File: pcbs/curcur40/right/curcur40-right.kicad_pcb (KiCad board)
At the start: 2 copper layers, 124.3 x 91.8 mm, 88 parts, among them U1 PMW3360DM-T2QU, U2 TLV74318PDBVR

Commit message: fix hole
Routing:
- net GNDR: track 248.1 -> 275.1 mm
- net /MISO: track 133.3 -> 133.8 mm
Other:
- outline, holes or cut-outs redrawn

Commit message: シルク文字
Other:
- board text added: "curcur40"

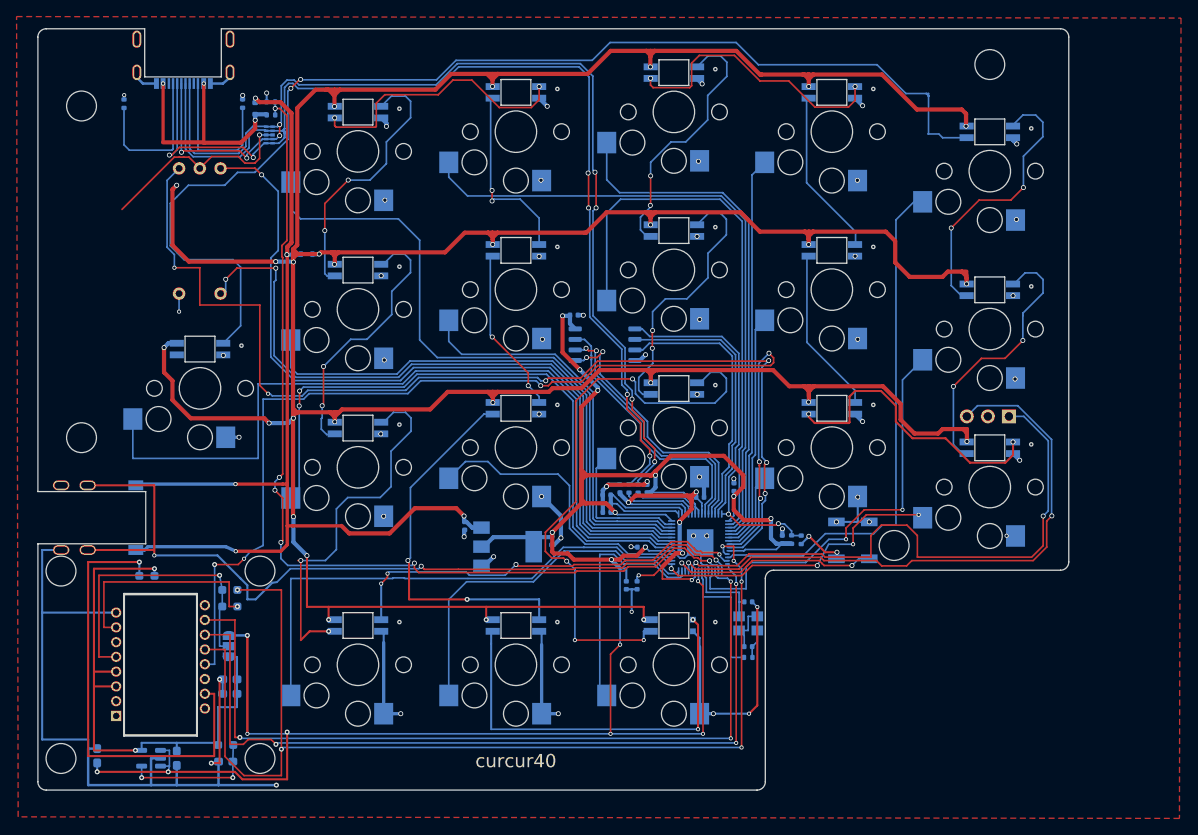
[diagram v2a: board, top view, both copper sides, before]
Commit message: fix(pcb): eliminate all ERC/DRC/parity warnings and ignored DRC checks on left and right PCBs
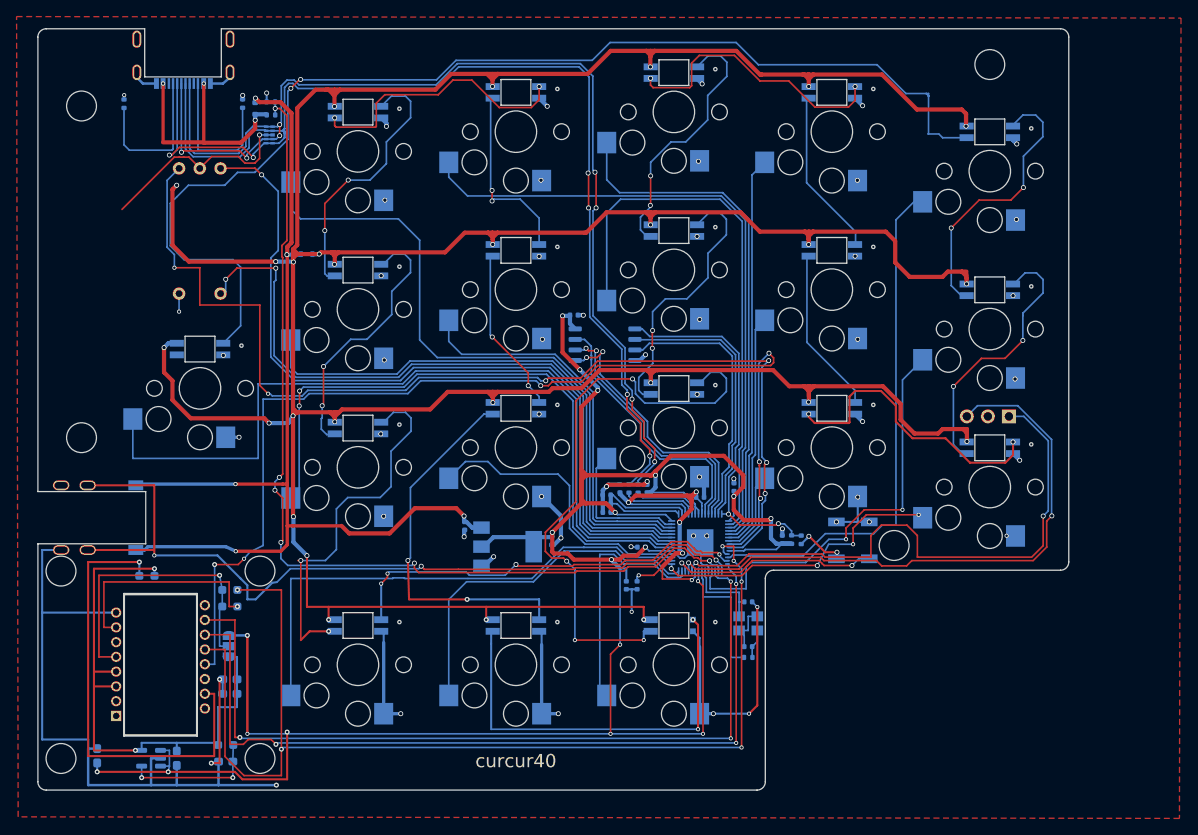
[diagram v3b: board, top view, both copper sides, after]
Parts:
- rLED9: footprint kbd_local:YS-SK6812MINI-E -> kbd_local:YS-SK6812MINI-E_rLED9
- rSW1: footprint kbd_local:keyswitch_choc12_hotswap_1u -> kbd_local:keyswitch_choc12_hotswap_1.5u
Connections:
- net +1V8_PMW renamed /+1V8_PMW
- net V_{IO} renamed /V_{IO}
- U1 pad 9: /MOTION -> unconnected-(U1-MOTION-Pad9)

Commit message: Refactor PCBs and schematics to use genuine KiCad 10.0 standard libraries and isolate PMW3360 VDDPIX
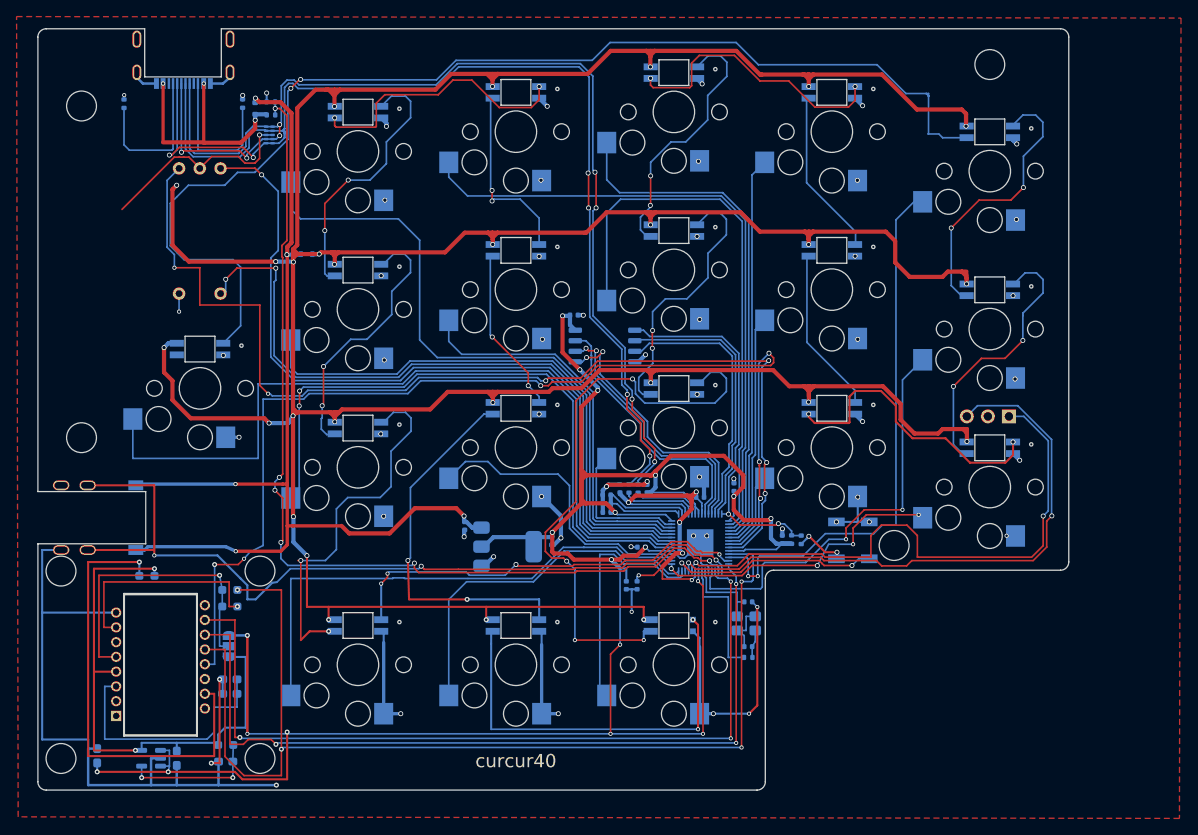
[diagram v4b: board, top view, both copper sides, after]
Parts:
- U1: footprint kbd_local:PMW3360DM-T2QU_16Pin -> kbd:PMW3360DM-T2QU_16Pin
- rEXLED2, rLED1, rLED10, rLED11, rLED12, rLED13, rLED14, rLED15, rLED16, rLED17, rLED18, rLED2, rLED3, rLED4, rLED5, rLED6, rLED7, rLED8: footprint kbd_local:YS-SK6812MINI-E -> kbd:YS-SK6812MINI-E
- rEXSW1: footprint kbd_local:CKW12 -> kbd:RotaryEncoder_Switch_CKW12
- rEXSW2, rSW10, rSW11, rSW12, rSW13, rSW14, rSW15, rSW16, rSW17, rSW18, rSW2, rSW3, rSW4, rSW5, rSW6, rSW7, rSW8, rSW9: footprint kbd_local:keyswitch_choc12_hotswap_1u -> kbd:keyswitch_choc12_hotswap_1u
- rJ1: footprint kbd_local:TYPE-C-31-M-13C -> kbd:USB_C_Receptacle_TYPE-C-31-M-13C
- rJ2: footprint kbd_local:PJ-398A-5A_PJ-399B-6A -> kbd:Jack_PJ-398A-5A_PJ-399B-6A
- rLED9: footprint kbd_local:YS-SK6812MINI-E_rLED9 -> kbd:YS-SK6812MINI-E_rLED9
- rSMDSW1, rSMDSW2: footprint kbd_local:TS-1088R-02026 -> kbd:TS-1088R-02026
- rSW1: footprint kbd_local:keyswitch_choc12_hotswap_1.5u -> kbd:keyswitch_choc12_hotswap_1.5u
- moved rY1 0.25 mm to (80.2, 47.4)
- moved rU4 0.16 mm to (63.1, 13.9)
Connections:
- C1 pad 1: /+1V8_PMW -> Net-(U1-VDDPIX)
- C2 pad 1: /+1V8_PMW -> Net-(U1-VDDPIX)
- U1 pad 3: /+1V8_PMW -> Net-(U1-VDDPIX)
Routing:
- net Net-(U1-VDDPIX): track 0.00 -> 30.4 mm
- net /KEY18: track 63.0 -> 67.1 mm, vias 0 -> 2
- net /+1V8_PMW: track 66.2 -> 65.1 mm
- net /MISO: track 133.8 -> 133.9 mm, vias 6 -> 4

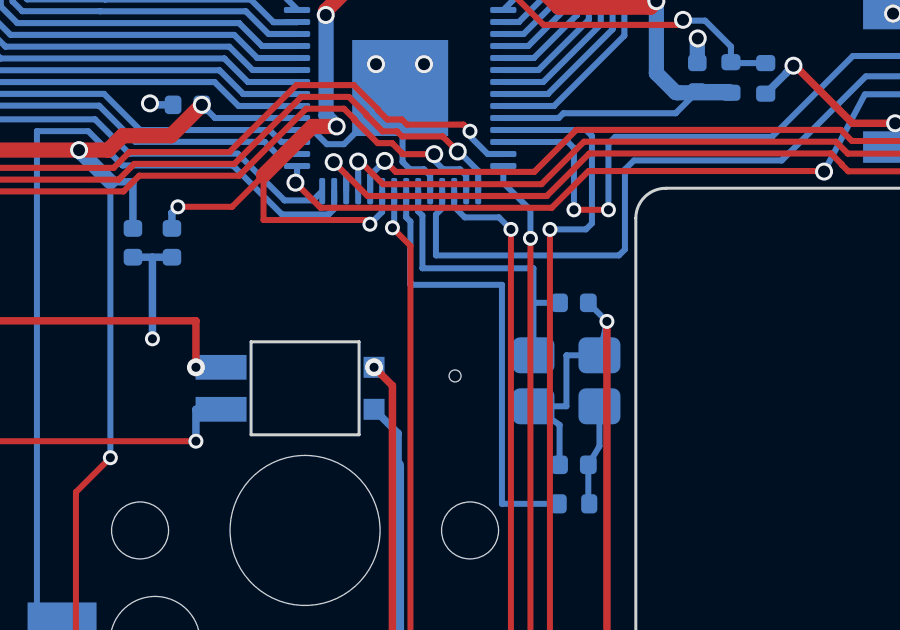
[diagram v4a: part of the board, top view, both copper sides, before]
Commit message: Clean up unused custom library files, fix fp-lib-table, and mark SWD headers J4/rJ4 as DNP
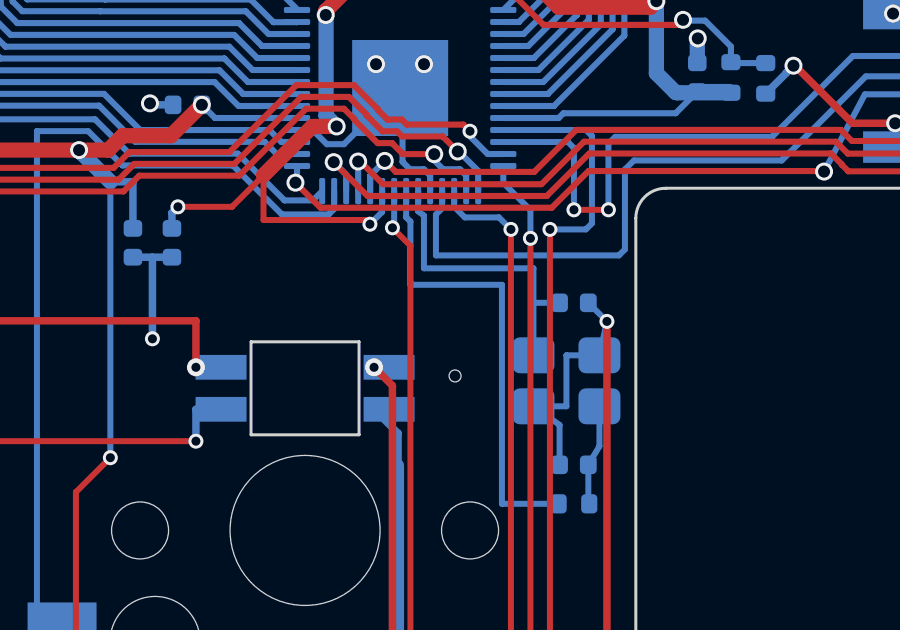
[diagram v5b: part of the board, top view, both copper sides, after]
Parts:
- rLED9: footprint kbd:YS-SK6812MINI-E_rLED9 -> kbd:YS-SK6812MINI-E

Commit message: Unify SW1/rSW1 to 1u Choc footprint and document curcur40 component specs and sourcing in pcb_spec.md
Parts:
- rSW1: footprint kbd:keyswitch_choc12_hotswap_1.5u -> kbd:keyswitch_choc12_hotswap_1u
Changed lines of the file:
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@@
 		)
 	)
-	(footprint "kbd:keyswitch_choc12_hotswap_1.5u"
+	(footprint "kbd:keyswitch_choc12_hotswap_1u"
 		(layer "B.Cu")
 		(at 33.3375 52.3875 180)
@@
 		)
 		(fp_line
-			(start 14.2875 9.525)
-			(end -14.2875 9.525)
+			(start 9.525 9.525)
+			(end -9.525 9.525)
 			(stroke
 				(width 0.1)
@@
 		)
 		(fp_line
-			(start 14.2875 -9.525)
-			(end 14.2875 9.525)
+			(start 9.525 -9.525)
+			(end 9.525 9.525)
 			(stroke
 				(width 0.1)
@@
 		)
 		(fp_line
-			(start -14.2875 9.525)
-			(end -14.2875 -9.525)
+			(start -9.525 9.525)
+			(end -9.525 -9.525)
 			(stroke
 				(width 0.1)
@@
 		)
 		(fp_line
-			(start -14.2875 -9.525)
-			(end 14.2875 -9.525)
+			(start -9.525 -9.525)
+			(end 9.525 -9.525)
 			(stroke
 				(width 0.1)

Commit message: Fix global pad_to_mask_clearance to 0mm, remove footprint solder_mask_margin overrides, and fix custom 3D model paths
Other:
- rule pad_to_mask_clearance: 0.2 -> 0

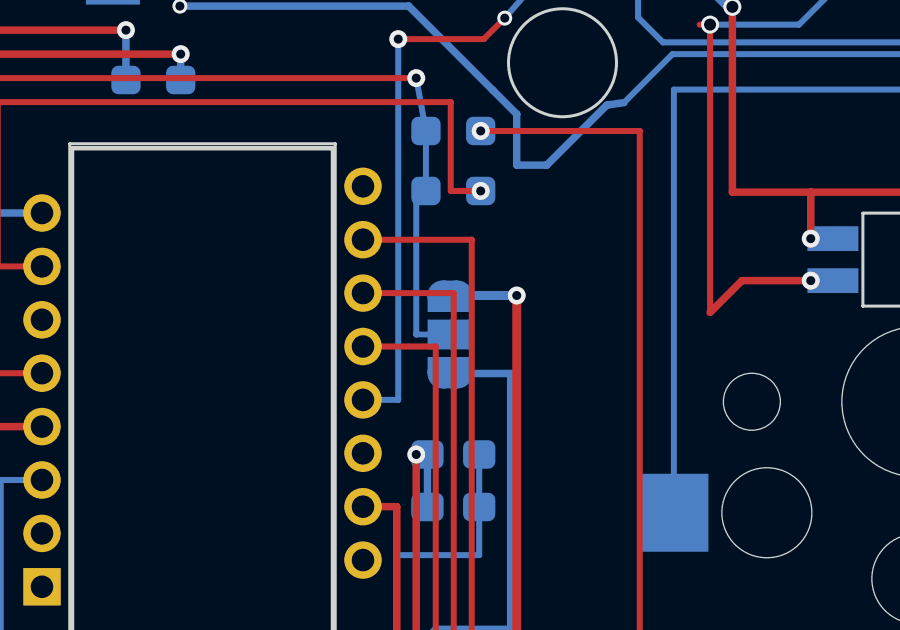
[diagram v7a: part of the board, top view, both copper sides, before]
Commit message: 1. 実施内容のまとめ
①・② 右手 PCB (curcur40-right) の JP1 直結化 ＆ R4 / C5 の DNP 化
JP1（電圧選択ジャンパ）の基板内パターン直結化:
curcur40-right.kicad_sch および curcur40-right.kicad_pcb の JP1 を、KiCad 10.0 標準のブリッジ済みシンボル・フットプリント（Jumper:SolderJumper_3_Bridged12 / Jumper:SolderJumper-3_P1.3mm_Bridged12_RoundedPad1.0x1.5mm_NumberLabels）に変更しました。
(net_tie_pad_groups "1, 2") と B.Cu 銅箔ポリゴンにより、Pad 1 (+3V3R) – Pad 2 (/V_{IO}) 間が最初から銅箔パターンで直結され、組み立て時のブリッジ忘れや逆ブリッジ（Pad 2–3 短絡）が物理的に起きない構造になっています。
R4 (28kΩ) と C5 (22nF) の DNP 化:
回路図・PCB の双方で DNP（未実装）・BOM 除外・CPL（実装座標）除外・3Dモデル非表示に設定しました。
あわせて、R1（10kΩ：/RESET プルアップ抵抗）に残っていた旧テンプレート由来の不要な dnp フラグを解除し、実装対象（C25804）として回路図・PCB・BOM/CPL の設定を統一しました。
１．ボトムプレートの削除・不要ファイルのクリーンアップ・スクリプト整理
ボトムプレート関連ファイルの完全削除:
plates/curcur40/pcb/plate-bottom* および plates/curcur40/pcb/jlcpcb/production_files/GERBER-plate-bottom* をすべて削除しました。
generate_plates.py およびレーザーカット用 plate-curcur40.svg からボトムプレート出力を削除し、左右トッププレートのみを出力するよう更新しました。
一時ファイル・スクラッチの削除:
scratch/, tmp/, .mypy_cache/, ルート直下の *_drc*.json, cases/curcur40/drc_check.rpt, cases/curcur40/right_pcb.step, 各 PCB/Plate フォルダ内の .rpt / .net / .bak* / .kicad_prl 等の作業用一時ファイルをすべて削除しました。
scripts/ フォルダの整理と格納ルールの策定:
恒久的に使用する公式ジェネレータ・エクスポータ 8本 に集約し、格納・運用ルールを scripts/README.md および pcb_spec.md 第9節 にまとめました：
generate_cases.py（左右ボトムケース STEP/STL 生成）
generate_trackball_cup.py（トラックボールカップ＆ボール付アセンブリ STEP/STL 生成）
generate_sensor_assemblies.py（光学センサー検証用 STEP 2種生成）
generate_full_assembly.py（フルアセンブリ STEP 生成＆全干渉検証）
generate_plates.py（左右トッププレート PCB/SVG 生成＆DRC検証）
export_jlcpcb.py（JLCPCB 発注用 Gerber ZIP / BOM CSV / CPL CSV 一括出力）
generate_spec_diagrams.py（仕様書用の断面・解説図版生成）
render_previews.py（ドキュメント用 3D プレビュー画像一括レンダリング）
２．4つの 3D モデル（STEP）へのレンズ側光学距離基準点のプロット

GUI（CAD Viewer 等）の計測ツール（📏 Measure）で直接クリック選択し、25mm ボール球面（Trackball_25mm, 最下面
𝑍
rel
=
+
5.80
 mm
Z
rel
	​

=+5.80 mm）との最短距離を計測した際に正確に設計値 2.40 mm が表示されるよう、光軸中心
(
𝑋
opt
,
𝑌
opt
)
(X
opt
	​

,Y
opt
	​

) のレンズフランジ着座高さ（
𝑍
rel
=
+
3.4000
 mm
Z
rel
	​

=+3.4000 mm / フルアセンブリ
𝑍
=
−
0.2000
 mm
Z=−0.2000 mm）に独立した名前付きオブジェクト Lens_Optical_Ref_Point（厚みゼ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
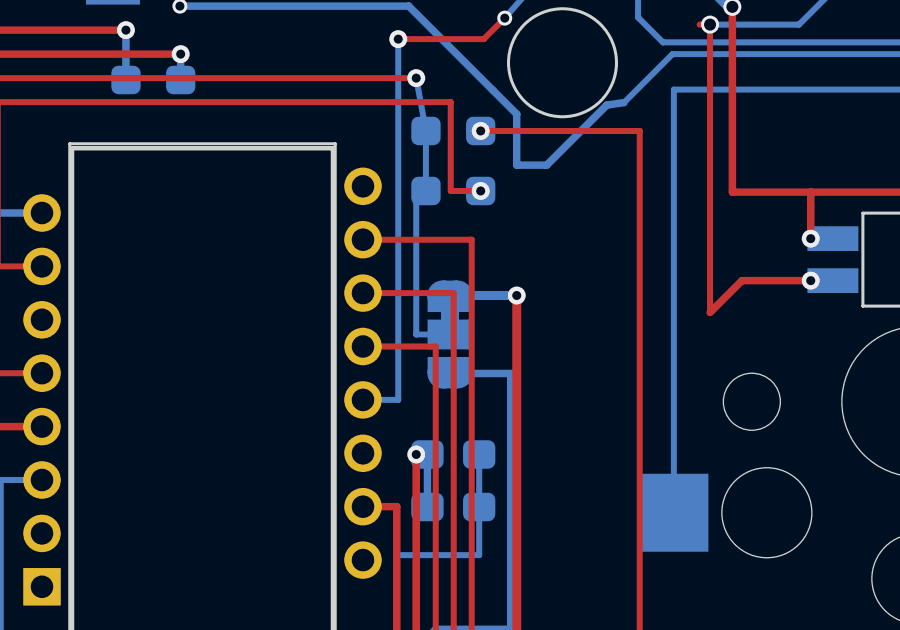
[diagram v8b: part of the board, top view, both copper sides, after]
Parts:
- JP1: value SolderJumper_3_Open -> SolderJumper_3_Bridged12; footprint Jumper:SolderJumper-3_P1.3mm_Open_RoundedPad1.0x1.5mm_NumberLabels -> Jumper:SolderJumper-3_P1.3mm_Bridged12_RoundedPad1.0x1.5mm_NumberLabels
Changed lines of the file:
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@@
 			)
 		)
-		(property "dnp" ""
-			(at 0 0 0)
-			(layer "B.SilkS")
-			(hide yes)
-			(effects
-				(font
-					(size 1.27 1.27)
-					(thickness 0.15)
-				)
-			)
-		)
-		(attr smd dnp)
+		(attr smd)
 		(duplicate_pad_numbers_are_jumpers no)
 		(fp_line
@@
 		)
 	)
-	(footprint "Jumper:SolderJumper-3_P1.3mm_Open_RoundedPad1.0x1.5mm_NumberLabels"
+	(footprint "Jumper:SolderJumper-3_P1.3mm_Bridged12_RoundedPad1.0x1.5mm_NumberLabels"
 		(layer "B.Cu")
 		(at 17.775 50.1457 -90)
-		(descr "SMD Solder 3-pad Jumper, 1x1.5mm rounded Pads, 0.3mm gap, open, labeled with numbers")
-		(tags "solder jumper open")
+		(descr "SMD Solder 3-pad Jumper, 1x1.5mm rounded Pads, 0.3mm gap, pads 1-2 bridged with 1 copper strip, labeled with numbers")
+		(tags "net tie solder jumper bridged")
 		(property "Reference" "JP1"
 			(at 0 2 90)
@@
 			)
 		)
-		(property "Value" "SolderJumper_3_Open"
+		(property "Value" "SolderJumper_3_Bridged12"
 			(at 0 -1.9 90)
 			(layer "B.Fab")
@@
 			)
 		)
-		(property "Description" "Solder Jumper, 3-pole, open"
+		(property "Description" "3-pole Solder Jumper, pins 1+2 closed/bridged"
 			(at 0 0 90)
 			(unlocked yes)
@@
 		(zone_connect 1)
 		(attr exclude_from_pos_files exclude_from_bom allow_soldermask_bridges)
+		(net_tie_pad_groups "1, 2")
 		(duplicate_pad_numbers_are_jumpers no)
+		(fp_poly
+			(pts
+				(xy -0.9 0.3) (xy -0.4 0.3) (xy -0.4 -0.3) (xy -0.9 -0.3)
+			)
+			(stroke
+				(width 0)
+				(type solid)
+			)
+			(fill yes)
+			(layer "B.Cu")
+		)
 		(fp_rect
 			(start -0.75 0.75)
@@
 			)
 			(primitives
+				(gr_poly
+					(pts
+						(xy 0.55 -0.75) (xy 0 -0.75) (xy 0 0.75) (xy 0.55 0.75)
+					)
+					(width 0)
+					(fill yes)
+				)
 				(gr_circle
 					(center 0 -0.25)
@@
 					(fill yes)
 				)
-				(gr_poly
-					(pts
-						(xy 0.55 -0.75) (xy 0 -0.75) (xy 0 0.75) (xy 0.55 0.75)
-					)
-					(width 0)
-					(fill yes)
-				)
 			)
 		)
@@
 			)
 		)
-		(attr smd dnp)
+		(attr smd exclude_from_pos_files exclude_from_bom dnp)
 		(duplicate_pad_numbers_are_jumpers no)
 		(fp_line
@@
 		)
 		(embedded_fonts no)
-		(model "${KICAD10_3DMODEL_DIR}/Capacitor_SMD.3dshapes/C_0603_1608Metric.step"
-			(offset
-				(xyz 0 0 0)
-			)
-			(scale
-				(xyz 1 1 1)
-			)
-			(rotate
-				(xyz 0 0 0)
-			)
-		)
 	)
 	(footprint "kbd:keyswitch_choc12_hotswap_1u"
@@
 			)
 		)
-		(attr smd dnp)
+		(attr smd exclude_from_pos_files exclude_from_bom dnp)
 		(duplicate_pad_numbers_are_jumpers no)
 		(fp_line
@@
 		)
 		(embedded_fonts no)
-		(model "${KICAD10_3DMODEL_DIR}/Resistor_SMD.3dshapes/R_0603_1608Metric.step"
-			(offset
-				(xyz 0 0 0)
-			)
-			(scale
-				(xyz 1 1 1)
-			)
-			(rotate
-				(xyz 0 0 0)
-			)
-		)
 	)
 	(footprint "kbd:keyswitch_choc12_hotswap_1u"
